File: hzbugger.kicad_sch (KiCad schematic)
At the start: 51 parts, among them J2 IDC, J4 SWD, J6 GPIO, SW1 RESET_SW, SW2 BOOT0_SW, U1 STM32F103C8T6, U2 SRV05-4, U3 AMS1117-3.3, U4 HX AM 90D, Y1 8M

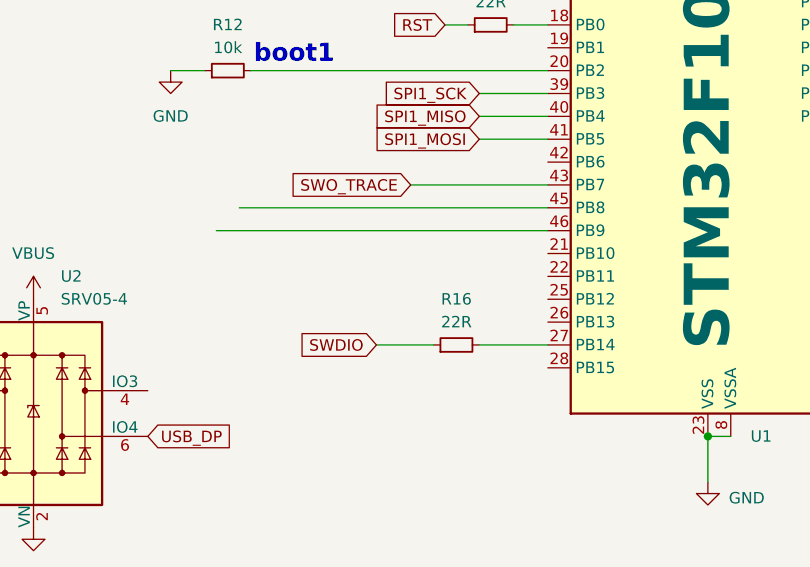
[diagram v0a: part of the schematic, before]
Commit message: usr led
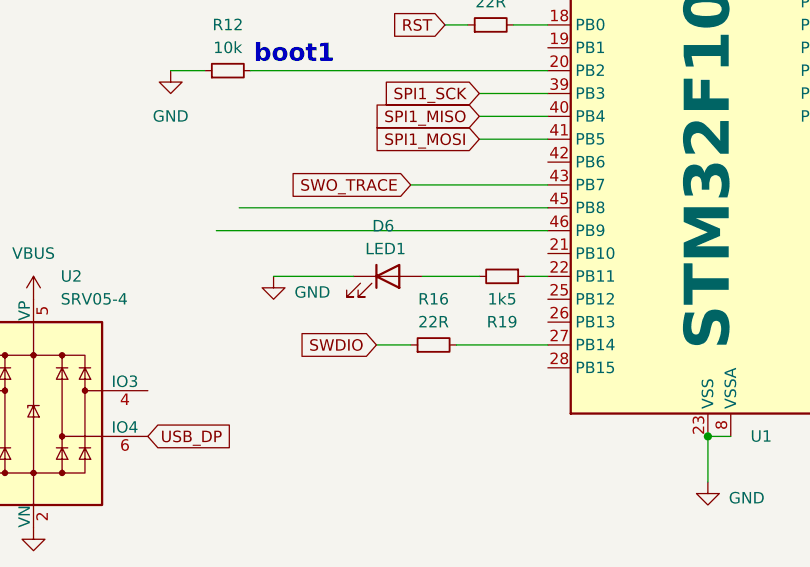
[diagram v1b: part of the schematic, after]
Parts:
- added D6: LED1, LED_SMD:LED_0603_1608Metric, symbol Device:LED
- added R19: 1k5, Resistor_SMD:R_0402_1005Metric, symbol Device:R_Small
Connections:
- net GND: now also D6.1 (K)
- net at U1.22 (PB11): now also R19.1
- new net: D6.2 (A), R19.2
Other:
- moved on the sheet: R16

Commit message: DRC
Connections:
- net +3V3: now also SW2.3 (C)
- net at SW2.1 (A): now also R8.1, SW2.2 (B), U1.44 (BOOT0)
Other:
- moved on the sheet: R8, SW2
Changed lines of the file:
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@@
 	)
 	(junction
+		(at 90.17 60.96)
+		(diameter 0)
+		(color 0 0 0 0)
+	)
+	(junction
+		(at 92.71 60.96)
+		(diameter 0)
+		(color 0 0 0 0)
+	)
+	(junction
 		(at 157.48 40.64)
 		(diameter 0)
@@
 	(wire
 		(pts
+			(xy 92.71 60.96) (xy 90.17 60.96)
+		)
+		(stroke
+			(width 0)
+			(type default)
+		)
+	)
+	(wire
+		(pts
 			(xy 273.05 30.48) (xy 269.24 30.48)
 		)
@@
 	(wire
 		(pts
+			(xy 90.17 60.96) (xy 81.28 60.96)
+		)
+		(stroke
+			(width 0)
+			(type default)
+		)
+	)
+	(wire
+		(pts
 			(xy 166.37 88.9) (xy 160.02 88.9)
 		)
@@
 	(wire
 		(pts
-			(xy 87.63 60.96) (xy 85.09 60.96)
+			(xy 76.2 60.96) (xy 72.39 60.96)
 		)
 		(stroke
@@
 	(wire
 		(pts
+			(xy 90.17 77.47) (xy 92.71 77.47)
+		)
+		(stroke
+			(width 0)
+			(type default)
+		)
+	)
+	(wire
+		(pts
 			(xy 109.22 44.45) (xy 109.22 46.99)
 		)
@@
 	(wire
 		(pts
+			(xy 92.71 77.47) (xy 92.71 60.96)
+		)
+		(stroke
+			(width 0)
+			(type default)
+		)
+	)
+	(wire
+		(pts
 			(xy 166.37 86.36) (xy 160.02 86.36)
 		)
@@
 	(wire
 		(pts
+			(xy 90.17 60.96) (xy 90.17 67.31)
+		)
+		(stroke
+			(width 0)
+			(type default)
+		)
+	)
+	(wire
+		(pts
 			(xy 269.24 30.48) (xy 259.08 30.48)
 		)
@@
 	(symbol
 		(lib_id "power:GND")
-		(at 85.09 60.96 0)
+		(at 72.39 60.96 0)
 		(unit 1)
 		(exclude_from_sim no)
@@
 		(fields_autoplaced yes)
 		(property "Reference" "#PWR53"
-			(at 85.09 67.31 0)
+			(at 72.39 67.31 0)
 			(effects
 				(font
@@
 		)
 		(property "Value" "GND"
-			(at 85.09 66.04 0)
+			(at 72.39 66.04 0)
 			(effects
 				(font
@@
 		)
 		(property "Footprint" ""
-			(at 85.09 60.96 0)
+			(at 72.39 60.96 0)
 			(effects
 				(font
@@
 		)
 		(property "Datasheet" ""
-			(at 85.09 60.96 0)
+			(at 72.39 60.96 0)
 			(effects
 				(font
@@
 		)
 		(property "Description" "Power symbol creates a global label with name \"GND\" , ground"
-			(at 85.09 60.96 0)
+			(at 72.39 60.96 0)
 			(effects
 				(font
@@
 	)
 	(symbol
+		(lib_id "power:+3V3")
+		(at 82.55 67.31 0)
+		(unit 1)
+		(exclude_from_sim no)
+		(in_bom yes)
+		(on_board yes)
+		(dnp no)
+		(property "Reference" "#PWR033"
+			(at 82.55 71.12 0)
+			(effects
+				(font
+					(size 1.27 1.27)
+				)
+				(hide yes)
+			)
+		)
+		(property "Value" "+3V3"
+			(at 86.106 65.278 0)
+			(effects
+				(font
+					(size 1.27 1.27)
+				)
+			)
+		)
+		(property "Footprint" ""
+			(at 82.55 67.31 0)
+			(effects
+				(font
+					(size 1.27 1.27)
+				)
+				(hide yes)
+			)
+		)
+		(property "Datasheet" ""
+			(at 82.55 67.31 0)
+			(effects
+				(font
+					(size 1.27 1.27)
+				)
+				(hide yes)
+			)
+		)
+		(property "Description" "Power symbol creates a global label with name \"+3V3\""
+			(at 82.55 67.31 0)
+			(effects
+				(font
+					(size 1.27 1.27)
+				)
+				(hide yes)
+			)
+		)
+		(pin "1"
+		)
+		(instances
+			(project "hzbugger"
+				(path "/493ccddd-ac13-43bb-97a7-ed9a2ed970cc"
+					(reference "#PWR033")
+					(unit 1)
+				)
+			)
+		)
+	)
+	(symbol
 		(lib_id "hzbugger:HXAM90D")
 		(at 45.72 90.17 0)
@@
 	(symbol
 		(lib_id "hzbugger:TS-1187A-B-A-B")
-		(at 66.04 58.42 270)
+		(at 87.63 72.39 270)
 		(unit 1)
 		(exclude_from_sim no)
@@
 		(dnp no)
 		(property "Reference" "SW2"
-			(at 47.752 57.658 90)
+			(at 75.184 71.628 90)
 			(effects
 				(font
@@
 		)
 		(property "Value" "BOOT0_SW"
-			(at 43.434 59.944 90)
+			(at 70.866 73.914 90)
 			(effects
 				(font
@@
 		)
 		(property "Footprint" "hzbugger:SW-SMD_4P-L5.1-W5.1-P3.70-LS6.5-TL_H1.5"
-			(at 53.34 58.42 0)
+			(at 74.93 72.39 0)
 			(effects
 				(font
@@
 		)
 		(property "Datasheet" "https://lcsc.com/product-detail/Tactile-Switches_XKB-Enterprise-TS-1187-B-A-A_C318884.html"
-			(at 50.8 58.42 0)
+			(at 72.39 72.39 0)
 			(effects
 				(font
@@
 		)
 		(property "Description" ""
-			(at 66.04 58.42 0)
+			(at 87.63 72.39 0)
 			(effects
 				(font
@@
 		)
 		(property "LCSC" "C318884"
-			(at 48.26 58.42 0)
+			(at 69.85 72.39 0)
 			(effects
 				(font
@@
 	(symbol
 		(lib_id "Device:R_Small")
-		(at 90.17 60.96 270)
+		(at 78.74 60.96 270)
 		(unit 1)
 		(exclude_from_sim no)
@@
 		(dnp no)
 		(property "Reference" "R8"
-			(at 89.662 65.024 90)
+			(at 78.232 65.024 90)
 			(effects
 				(font
@@
 		)
 		(property "Value" "10k"
-			(at 89.916 62.992 90)
+			(at 78.486 62.992 90)
 			(effects
 				(font
@@
 		)
 		(property "Footprint" "Resistor_SMD:R_0402_1005Metric"
-			(at 90.17 60.96 0)
+			(at 78.74 60.96 0)
 			(effects
 				(font
@@
 		)
 		(property "Datasheet" "~"
-			(at 90.17 60.96 0)
+			(at 78.74 60.96 0)
 			(effects
 				(font
@@
 		)
 		(property "Description" "Resistor, small symbol"
-			(at 90.17 60.96 0)
+			(at 78.74 60.96 0)
 			(effects
 				(font
@@
 		)
 		(property "LCSC" "C25744"
-			(at 90.17 60.96 0)
+			(at 78.74 60.96 0)
 			(effects
 				(font

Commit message: IDC pad lengths
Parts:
- D1, D6: footprint LED_SMD:LED_0603_1608Metric -> LED_SMD:LED_0805_2012Metric
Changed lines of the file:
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@@
 			)
 		)
-		(property "Footprint" "LED_SMD:LED_0603_1608Metric"
+		(property "Footprint" "LED_SMD:LED_0805_2012Metric"
 			(at 248.92 100.33 0)
 			(effects
@@
 			)
 		)
-		(property "Footprint" "LED_SMD:LED_0603_1608Metric"
+		(property "Footprint" "LED_SMD:LED_0805_2012Metric"
 			(at 106.68 111.76 0)
 			(effects

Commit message: some final adjustments
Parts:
- R11: footprint Resistor_SMD:R_0402_1005Metric -> Resistor_SMD:R_0402_1005Metric_Pad0.72x0.64mm_HandSolder
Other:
- note added: "LED silk markings!"
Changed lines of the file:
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@@
 		)
 	)
+	(text "LED silk \nmarkings!"
+		(exclude_from_sim no)
+		(at 106.172 145.796 0)
+		(effects
+			(font
+				(size 6 6)
+				(thickness 1.2)
+				(bold yes)
+			)
+		)
+	)
 	(junction
 		(at 83.82 33.02)
@@
 			)
 		)
-		(property "Footprint" "Resistor_SMD:R_0402_1005Metric"
+		(property "Footprint" "Resistor_SMD:R_0402_1005Metric_Pad0.72x0.64mm_HandSolder"
 			(at 203.2 82.55 0)
 			(effects

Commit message: tx led
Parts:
- added D7: LED1, LED_SMD:LED_0603_1608Metric, symbol Device:LED
- added R20: 1k5, Resistor_SMD:R_0402_1005Metric, symbol Device:R_Small
- D1: LCSC (none) -> C2297
- D3: LCSC (none) -> C2286
- D4: LCSC (none) -> C2290
- J2, J4, J6, TP1, TP2: LCSC (none) -> DNP
- R13, R18, R19, R3, R6: LCSC (none) -> C22843
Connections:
- net +3V3: now also D7.2 (A)
- net UART_TX: now also R20.1
- new net: D7.1 (K), R20.2
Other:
- note removed: "LED silk markings!"
- note removed: "UART TX & RX LEDs?"
- moved on the sheet: TP1

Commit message: some enhancements, corrected LCSC code for 0422 1k5 R
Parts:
- R11, R13, R18, R19, R20, R3: LCSC C22843 -> C25867
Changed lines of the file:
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@@
 		)
 		(instances
-			(project ""
+			(project "hzbugger"
 				(path "/493ccddd-ac13-43bb-97a7-ed9a2ed970cc"
 					(reference "F1")
@@
 			)
 		)
-		(property "LCSC" "C22843"
+		(property "LCSC" "C25867"
 			(at 240.03 64.77 0)
 			(effects
@@
 		)
 		(instances
-			(project ""
+			(project "hzbugger"
 				(path "/493ccddd-ac13-43bb-97a7-ed9a2ed970cc"
 					(reference "Y1")
@@
 		)
 		(instances
-			(project ""
+			(project "hzbugger"
 				(path "/493ccddd-ac13-43bb-97a7-ed9a2ed970cc"
 					(reference "#PWR1")
@@
 		)
 		(instances
-			(project ""
+			(project "hzbugger"
 				(path "/493ccddd-ac13-43bb-97a7-ed9a2ed970cc"
 					(reference "TP1")
@@
 		)
 		(instances
-			(project ""
+			(project "hzbugger"
 				(path "/493ccddd-ac13-43bb-97a7-ed9a2ed970cc"
 					(reference "C8")
@@
 			)
 		)
-		(property "LCSC" "C22843"
+		(property "LCSC" "C25867"
 			(at 240.03 77.47 0)
 			(effects
@@
 		)
 		(instances
-			(project ""
+			(project "hzbugger"
 				(path "/493ccddd-ac13-43bb-97a7-ed9a2ed970cc"
 					(reference "SW1")
@@
 		)
 		(instances
-			(project ""
+			(project "hzbugger"
 				(path "/493ccddd-ac13-43bb-97a7-ed9a2ed970cc"
 					(reference "U4")
@@
 		)
 		(instances
-			(project ""
+			(project "hzbugger"
 				(path "/493ccddd-ac13-43bb-97a7-ed9a2ed970cc"
 					(reference "#PWR3")
@@
 			)
 		)
-		(property "LCSC" "C22843"
+		(property "LCSC" "C25867"
 			(at 181.61 54.61 0)
 			(effects
@@
 			)
 		)
-		(property "LCSC" "C22843"
+		(property "LCSC" "C25867"
 			(at 179.07 76.2 0)
 			(effects
@@
 		)
 		(instances
-			(project ""
+			(project "hzbugger"
 				(path "/493ccddd-ac13-43bb-97a7-ed9a2ed970cc"
 					(reference "#PWR5")
@@
 		)
 		(instances
-			(project ""
+			(project "hzbugger"
 				(path "/493ccddd-ac13-43bb-97a7-ed9a2ed970cc"
 					(reference "#PWR12")
@@
 		)
 		(instances
-			(project ""
+			(project "hzbugger"
 				(path "/493ccddd-ac13-43bb-97a7-ed9a2ed970cc"
 					(reference "J4")
@@
 		)
 		(instances
-			(project ""
+			(project "hzbugger"
 				(path "/493ccddd-ac13-43bb-97a7-ed9a2ed970cc"
 					(reference "J2")
@@
 			)
 		)
-		(property "LCSC" "C22843"
+		(property "LCSC" "C25867"
 			(at 119.38 111.76 0)
 			(effects
@@
 		)
 		(instances
-			(project ""
+			(project "hzbugger"
 				(path "/493ccddd-ac13-43bb-97a7-ed9a2ed970cc"
 					(reference "D1")
@@
 			)
 		)
-		(property "LCSC" "C22843"
+		(property "LCSC" "C25867"
 			(at 203.2 82.55 0)
 			(effects
@@
 		)
 		(instances
-			(project ""
+			(project "hzbugger"
 				(path "/493ccddd-ac13-43bb-97a7-ed9a2ed970cc"
 					(reference "U2")
@@
 		)
 		(instances
-			(project ""
+			(project "hzbugger"
 				(path "/493ccddd-ac13-43bb-97a7-ed9a2ed970cc"
 					(reference "U3")
@@
 		)
 		(instances
-			(project ""
+			(project "hzbugger"
 				(path "/493ccddd-ac13-43bb-97a7-ed9a2ed970cc"
 					(reference "U1")
@@
 		)
 		(instances
-			(project ""
+			(project "hzbugger"
 				(path "/493ccddd-ac13-43bb-97a7-ed9a2ed970cc"
 					(reference "D2")
